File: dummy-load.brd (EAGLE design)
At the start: 114.3 x 68.2 mm, 71 parts, among them T1 BU931P, T2 BU931P, T3 BU931P, T4 BU931P, T5 BU931P, T6 BU931P, T7 BU931P, T8 BU931P, U1 TLV272CD, U10 MCP4725A0T-E/CH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

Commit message: PCB routing
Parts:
- moved R29 146.8 mm to (9.84, 45.4), turned to 90 degrees
- moved R30 145.4 mm to (5.71, 45.4), turned to 270 degrees
- moved R27 44.9 mm to (103.5, 32.1), turned to 270 degrees
- moved R28 44.8 mm to (101.3, 32.1), turned to 270 degrees
- moved C9 35.5 mm to (94.0, 5.08), turned to 270 degrees
- moved R25 34.0 mm to (99.1, 14.6)
- moved R26 32.8 mm to (94.9, 14.6)
- moved C10 32.4 mm to (94.0, 11.1), turned to 270 degrees
- moved U10 19.5 mm to (98.1, 11.1)
- moved U9 19.3 mm to (98.1, 5.08)
- moved R2 8.28 mm to (66.0, 50.8), turned to 180 degrees
- moved R1 8.28 mm to (87.6, 50.8), turned to 180 degrees
- moved R3 8.28 mm to (44.5, 50.8), turned to 180 degrees
- moved R4 8.28 mm to (22.9, 50.8), turned to 180 degrees
- moved R13 8.01 mm to (84.1, 17.8), turned to 0 degrees
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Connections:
- net A1: now also X1.1; no longer X1.9
- net A2: now also X1.2; no longer X1.10
- net A3: now also X1.3; no longer X1.11
- net A4: now also X1.4; no longer X1.12
- net A5: now also X1.16; no longer X1.13
- net A6: now also X1.15; no longer X1.14
- net A7: now also X1.14; no longer X1.15
- net A8: now also X1.13; no longer X1.16
- net I1: now also X1.5; no longer X1.1
- net I2: now also X1.6; no longer X1.2
- net I3: now also X1.7; no longer X1.3
- net I4: now also X1.8; no longer X1.4
- net I5: now also X1.12; no longer X1.5
- net I6: now also X1.11; no longer X1.6
- net I7: now also X1.10; no longer X1.7
- net I8: now also X1.9; no longer X1.8
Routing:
- net +3V3: track 2.64 -> 415.3 mm, vias 0 -> 6
- net AGND: track 35.5 -> 386.3 mm, vias 0 -> 2
- net VACT: track 1.97 -> 251.6 mm, vias 1 -> 11
- net VSET: track 1.84 -> 207.2 mm, vias 1 -> 10
- net N$1: track 0.00 -> 156.6 mm, vias 0 -> 1
- net I8: track 0.00 -> 119.0 mm, vias 0 -> 1
- net A8: track 0.00 -> 118.3 mm, vias 0 -> 1
- net I7: track 0.00 -> 99.9 mm, vias 0 -> 1
- net A7: track 0.00 -> 99.1 mm, vias 0 -> 1
- net I4: track 0.00 -> 88.6 mm, vias 0 -> 1
- net A4: track 0.00 -> 88.3 mm, vias 0 -> 1
- net I6: track 0.00 -> 74.6 mm, vias 0 -> 1
- net A6: track 0.00 -> 73.7 mm, vias 0 -> 1
- net I3: track 0.00 -> 63.4 mm, vias 0 -> 1
- net A3: track 0.00 -> 63.1 mm, vias 0 -> 1
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
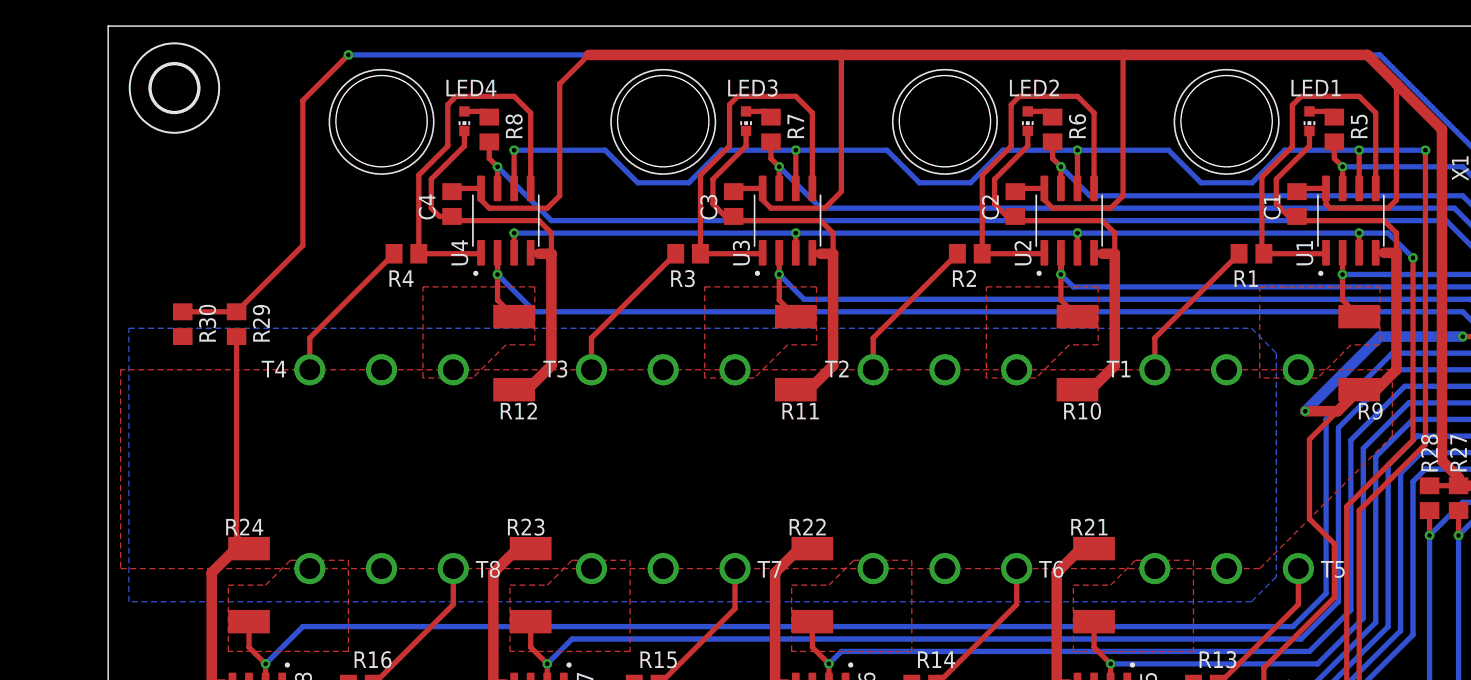
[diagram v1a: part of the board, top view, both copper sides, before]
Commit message: Add XT60 connector
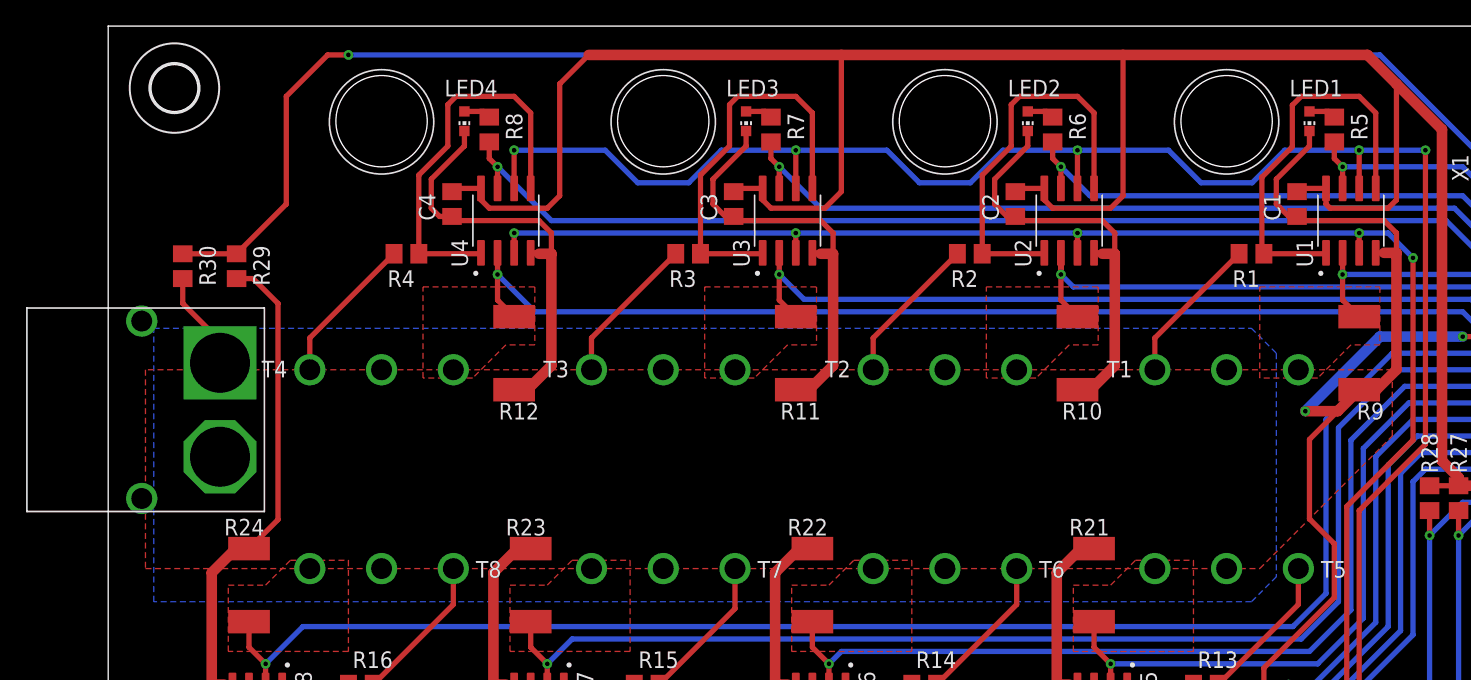
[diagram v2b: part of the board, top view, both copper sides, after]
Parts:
- added P1: XT60M-H, dummy-load:XT60M-H
- moved R29 4.44 mm to (9.84, 49.8)
- moved R30 4.44 mm to (5.71, 49.8)
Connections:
- net AGND: now also P1.-
- net VCC: now also P1.+
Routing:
- net VCC: track 0.00 -> 7.64 mm
- net AGND: track 386.3 -> 393.3 mm
- net N$1: track 156.6 -> 153.1 mm
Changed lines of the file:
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@@
 <attribute name="SPICEPREFIX" value="R" x="8.5725" y="-22.5425" size="1.778" layer="27" rot="R270" display="off"/>
 </element>
-<element name="R29" library="rcl" library_urn="urn:adsk.eagle:library:334" package="R0805" package3d_urn="urn:adsk.eagle:package:23553/2" value="10k" x="9.8425" y="45.4025" smashed="yes" rot="R90">
-<attribute name="NAME" x="11.1125" y="46.99" size="1.27" layer="25" rot="R270"/>
-<attribute name="POPULARITY" value="86" x="102.5525" y="106.3625" size="1.778" layer="27" rot="R90" display="off"/>
-<attribute name="SPICEPREFIX" value="R" x="102.5525" y="106.3625" size="1.778" layer="27" rot="R90" display="off"/>
+<element name="R29" library="rcl" library_urn="urn:adsk.eagle:library:334" package="R0805" package3d_urn="urn:adsk.eagle:package:23553/2" value="10k" x="9.8425" y="49.8475" smashed="yes" rot="R90">
+<attribute name="NAME" x="11.1125" y="51.435" size="1.27" layer="25" rot="R270"/>
+<attribute name="POPULARITY" value="86" x="102.5525" y="110.8075" size="1.778" layer="27" rot="R90" display="off"/>
+<attribute name="SPICEPREFIX" value="R" x="102.5525" y="110.8075" size="1.778" layer="27" rot="R90" display="off"/>
 </element>
 <element name="R3" library="rcl" library_urn="urn:adsk.eagle:library:334" package="R0805" package3d_urn="urn:adsk.eagle:package:23553/2" value="150" x="44.45" y="50.8" smashed="yes" rot="R180">
@@
 <attribute name="SPICEPREFIX" value="R" x="-31.75" y="143.51" size="1.778" layer="27" rot="R180" display="off"/>
 </element>
-<element name="R30" library="rcl" library_urn="urn:adsk.eagle:library:334" package="R0805" package3d_urn="urn:adsk.eagle:package:23553/2" value="330k" x="5.715" y="45.4025" smashed="yes" rot="R270">
-<attribute name="NAME" x="6.985" y="46.99" size="1.27" layer="25" rot="R270"/>
-<attribute name="POPULARITY" value="86" x="-73.025" y="-34.6075" size="1.778" layer="27" rot="R270" display="off"/>
-<attribute name="SPICEPREFIX" value="R" x="-73.025" y="-34.6075" size="1.778" layer="27" rot="R270" display="off"/>
+<element name="R30" library="rcl" library_urn="urn:adsk.eagle:library:334" package="R0805" package3d_urn="urn:adsk.eagle:package:23553/2" value="330k" x="5.715" y="49.8475" smashed="yes" rot="R270">
+<attribute name="NAME" x="6.985" y="51.435" size="1.27" layer="25" rot="R270"/>
+<attribute name="POPULARITY" value="86" x="-73.025" y="-30.1625" size="1.778" layer="27" rot="R270" display="off"/>
+<attribute name="SPICEPREFIX" value="R" x="-73.025" y="-30.1625" size="1.778" layer="27" rot="R270" display="off"/>
 </element>
 <element name="R4" library="rcl" library_urn="urn:adsk.eagle:library:334" package="R0805" package3d_urn="urn:adsk.eagle:package:23553/2" value="150" x="22.86" y="50.8" smashed="yes" rot="R180">
@@
 <attribute name="POPULARITY" value="2" x="109.22" y="63.5" size="1.778" layer="27" display="off"/>
 </element>
+<element name="P1" library="dummy-load" package="XT60M-H" value="XT60M-H" x="8.5725" y="35.2425" smashed="yes" rot="R90"/>
 </elements>
 <signals>
@@
 <contactref element="R29" pad="1"/>
 <polygon width="0.8128" layer="1" isolate="0.8128" rank="2">
-<vertex x="0.9525" y="26.67"/>
+<vertex x="2.8575" y="26.67"/>
 <vertex x="88.265" y="26.67"/>
 <vertex x="98.425" y="36.83"/>
 <vertex x="98.425" y="41.91"/>
-<vertex x="0.9525" y="41.91"/>
+<vertex x="2.8575" y="41.91"/>
 </polygon>
 <wire x1="97.155" y1="50.87" x2="97.225" y2="50.8" width="0.4064" layer="1"/>
@@
 <wire x1="88.5825" y1="19.05" x2="93.98" y2="24.4475" width="0.4064" layer="1"/>
 <wire x1="93.98" y1="24.4475" x2="93.98" y2="28.575" width="0.4064" layer="1"/>
-<wire x1="9.8425" y1="44.4525" x2="9.8425" y2="29.1525" width="0.4064" layer="1"/>
-<wire x1="9.8425" y1="29.1525" x2="10.795" y2="28.2" width="0.4064" layer="1"/>
 <wire x1="110.49" y1="33.02" x2="111.125" y2="33.02" width="0.8128" layer="1"/>
 <wire x1="111.125" y1="33.02" x2="112.395" y2="34.29" width="0.8128" layer="1"/>
@@
 <via x="91.7575" y="38.735" extent="1-16" drill="0.35"/>
 <wire x1="97.4725" y1="44.45" x2="91.7575" y2="38.735" width="0.8128" layer="16"/>
+<contactref element="P1" pad="-"/>
+<wire x1="13.0175" y1="46.9925" x2="11.1125" y2="48.8975" width="0.4064" layer="1"/>
+<wire x1="9.8425" y1="48.8975" x2="11.1125" y2="48.8975" width="0.4064" layer="1"/>
+<wire x1="13.0175" y1="30.4225" x2="10.795" y2="28.2" width="0.4064" layer="1"/>
+<wire x1="13.0175" y1="46.9925" x2="13.0175" y2="30.4225" width="0.4064" layer="1"/>
 </signal>
 <signal name="N$2">
@@
 <contactref element="R30" pad="2"/>
 <polygon width="0.8128" layer="16" isolate="0.8128">
-<vertex x="1.5875" y="45.085"/>
+<vertex x="3.4925" y="45.085"/>
 <vertex x="87.63" y="45.085"/>
 <vertex x="89.535" y="43.18"/>
 <vertex x="89.535" y="26.035"/>
 <vertex x="87.63" y="24.13"/>
-<vertex x="1.5875" y="24.13"/>
+<vertex x="3.4925" y="24.13"/>
 </polygon>
-<wire x1="20.955" y1="41.91" x2="5.715" y2="44.4525" width="0" layer="19" extent="1-1"/>
+<contactref element="P1" pad="+"/>
+<wire x1="8.5725" y1="44.135" x2="5.715" y2="46.9925" width="0.4064" layer="1"/>
+<wire x1="5.715" y1="48.8975" x2="5.715" y2="46.9925" width="0.4064" layer="1"/>
+<wire x1="8.5725" y1="44.135" x2="8.5725" y2="42.4425" width="0.4064" layer="1"/>
 </signal>
 <signal name="I5">
@@
 <contactref element="X1" pad="24"/>
 <contactref element="R30" pad="1"/>
-<wire x1="5.715" y1="46.3525" x2="9.8425" y2="46.3525" width="0.4064" layer="1"/>
-<wire x1="9.8425" y1="46.3525" x2="14.9225" y2="51.4325" width="0.4064" layer="1"/>
-<wire x1="14.9225" y1="62.5475" x2="18.415" y2="66.04" width="0.4064" layer="1"/>
 <via x="18.415" y="66.04" extent="1-16" drill="0.35"/>
 <wire x1="18.415" y1="66.04" x2="97.4725" y2="66.04" width="0.4064" layer="16"/>
 <wire x1="110.8075" y1="57.15" x2="112.395" y2="55.5625" width="0.4064" layer="16"/>
 <wire x1="112.395" y1="27.305" x2="110.49" y2="25.4" width="0.4064" layer="16"/>
-<wire x1="14.9225" y1="51.4325" x2="14.9225" y2="62.5475" width="0.4064" layer="1"/>
 <wire x1="97.4725" y1="66.04" x2="106.3625" y2="57.15" width="0.4064" layer="16"/>
 <wire x1="106.3625" y1="57.15" x2="110.8075" y2="57.15" width="0.4064" layer="16"/>
 <wire x1="112.395" y1="55.5625" x2="112.395" y2="27.305" width="0.4064" layer="16"/>
+<wire x1="5.715" y1="50.7975" x2="9.8425" y2="50.7975" width="0.4064" layer="1"/>
+<wire x1="9.8425" y1="50.7975" x2="13.6525" y2="54.6075" width="0.4064" layer="1"/>
+<wire x1="13.6525" y1="62.865" x2="16.8275" y2="66.04" width="0.4064" layer="1"/>
+<wire x1="16.8275" y1="66.04" x2="18.415" y2="66.04" width="0.4064" layer="1"/>
+<wire x1="13.6525" y1="54.6075" x2="13.6525" y2="62.865" width="0.4064" layer="1"/>
 </signal>
 </signals>
